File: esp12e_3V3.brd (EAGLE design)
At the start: 50 x 50 mm, 30 parts, among them CN1 1X4-CLEANBIG, CN2 1X4-CLEANBIG, CN3 1X4-CLEANBIG, IC1 117\33

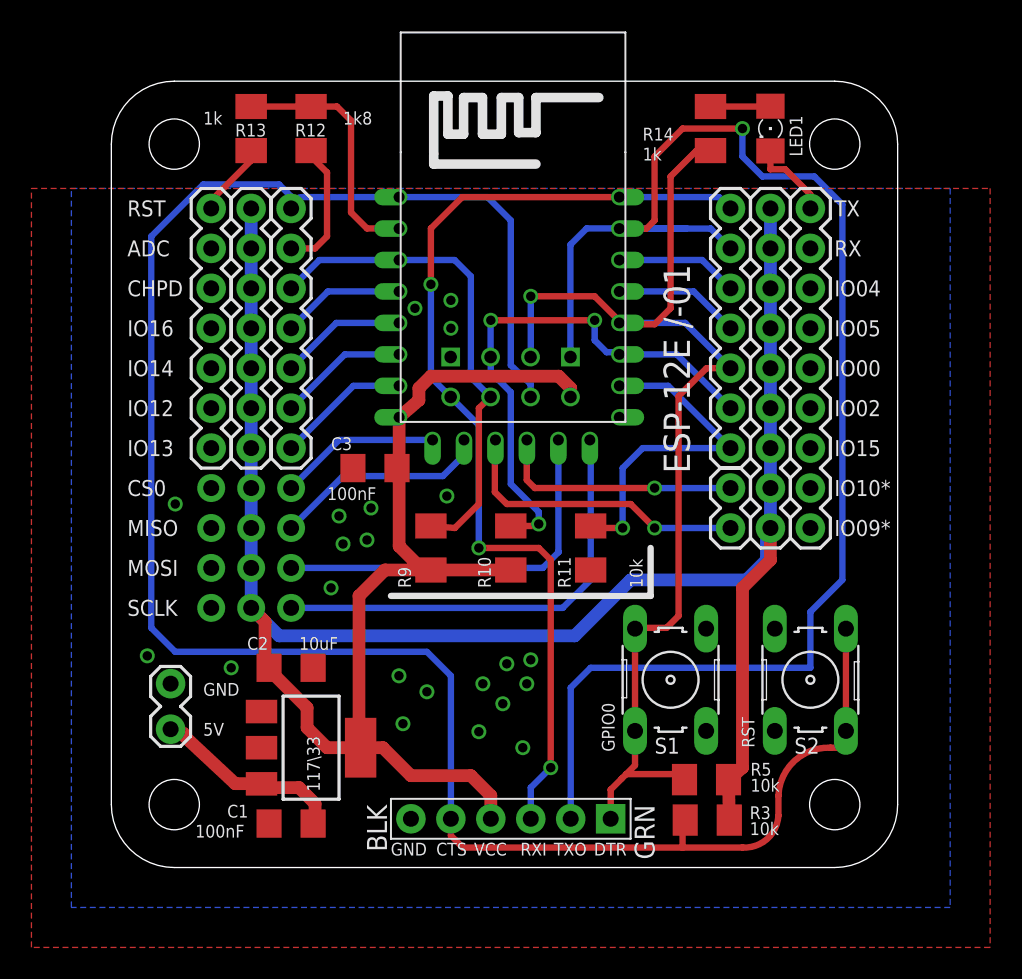
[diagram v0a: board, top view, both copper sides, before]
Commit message: moved 5V header, ftdi and added micro usbfootprint
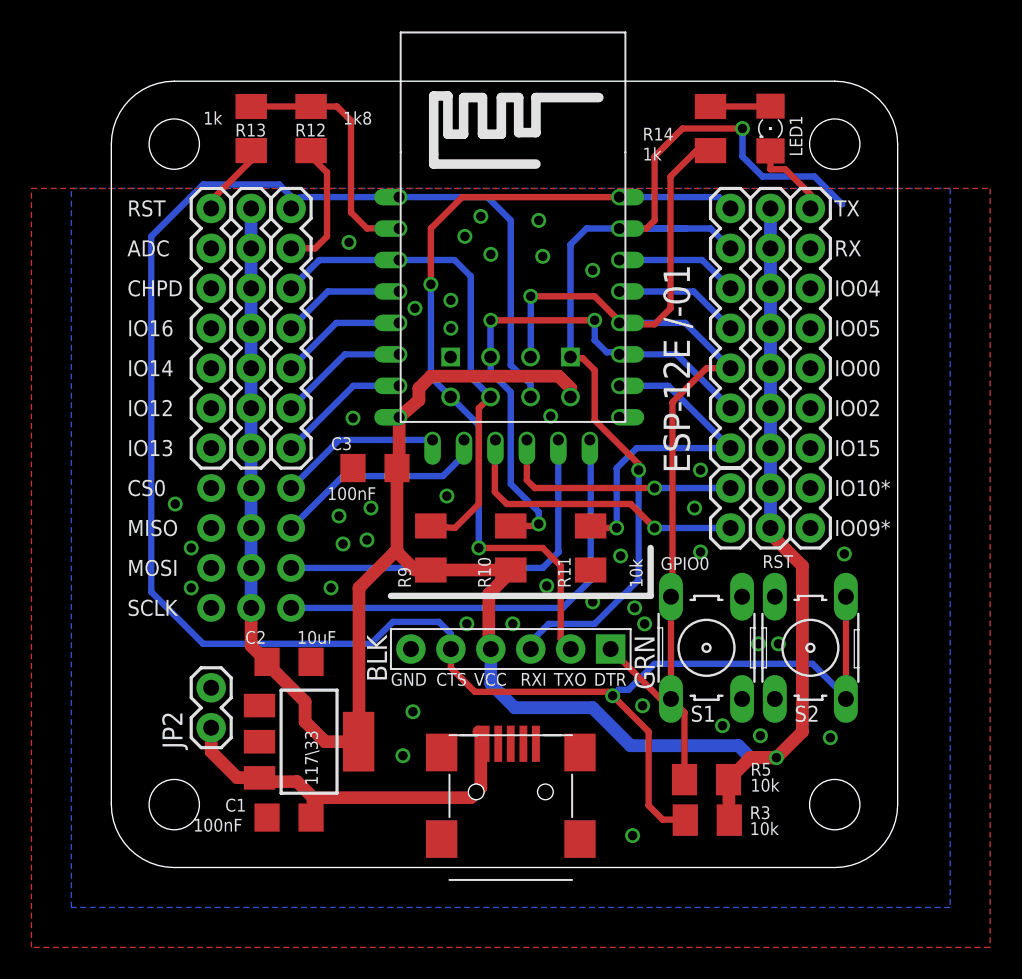
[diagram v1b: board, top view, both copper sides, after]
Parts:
- added CN4: (no value), adafruit:USB-MINIB
- JP2: value M02LOCK -> M02PTH; device SparkFun-Connectors:1X02_LOCK -> SparkFun-Connectors:1X02
- moved JP1 10.8 mm to (25.4, 13.9)
- moved S1 3.06 mm to (37.8, 14.0)
- moved JP2 2.58 mm to (6.35, 8.89)
- moved S2 2.03 mm to (44.5, 14.0)
- moved C2 0.40 mm to (11.3, 13.1)
- moved C1 0.40 mm to (11.3, 3.17)
- moved IC1 0.40 mm to (12.6, 8.00)
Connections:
- removed net FRX_ETX: JP1.P$3, JP5.1, U$2.TX, U$3.TX
- removed net FTX_ERX: JP1.P$2, JP5.2, U$2.RX, U$3.RX
- new net ERX: JP1.P$3, JP5.2, U$2.RX, U$3.RX
- new net ETX: JP1.P$2, JP5.1, U$2.TX, U$3.TX
- net GND: now also CN4.GND
- net VCC: now also CN4.VBUS
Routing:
- net FTX_ERX: track 100.0 -> 0.00 mm, vias 1 -> 0
- net ERX: track 0.00 -> 70.9 mm, vias 0 -> 2
- net FRX_ETX: track 63.6 -> 0.00 mm, vias 3 -> 0
- net ETX: track 0.00 -> 53.0 mm, vias 0 -> 2
- net +3V3: track 175.0 -> 153.8 mm, vias 0 -> 1
- net VCC: track 13.9 -> 26.3 mm
- net GPIO0: track 71.8 -> 68.0 mm
- net N$1: track 131.4 -> 128.9 mm, vias 0 -> 1
- net GND: vias 22 -> 41
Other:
- board text removed: "5V"
- board text removed: "GND"

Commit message: moved stuff
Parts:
- removed CN4: (no value), adafruit:USB-MINIB
- added JP3: USB_MICROB_PLUGCONN-11752, SparkFun-Connectors:USB-B-MICRO-SMD_V03
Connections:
- net GND: now also JP3.GND1; no longer CN4.GND
- net VCC: now also JP3.VBUS1; no longer CN4.VBUS
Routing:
- net VCC: track 26.3 -> 25.1 mm
- net GND: vias 41 -> 48
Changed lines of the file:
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@@
 <element name="CN2" library="adafruit" package="1X04-CLEANBIG" value="1X4-CLEANBIG" x="8.89" y="20.32" smashed="yes" rot="R90"/>
 <element name="CN3" library="adafruit" package="1X04-CLEANBIG" value="1X4-CLEANBIG" x="6.35" y="20.32" smashed="yes" rot="R90"/>
-<element name="CN4" library="adafruit" package="USB-MINIB" value="" x="25.4" y="3.81" smashed="yes">
-<attribute name="VALUE" x="22.09" y="-2.54" size="1.27" layer="27"/>
+<element name="JP2" library="SparkFun-Connectors" package="1X02" value="M02PTH" x="6.35" y="8.89" smashed="yes" rot="R90">
+<attribute name="NAME" x="4.5212" y="7.5438" size="0.8128" layer="25" font="vector" ratio="10" rot="R90"/>
+<attribute name="VALUE" x="9.525" y="7.62" size="1.27" layer="27" rot="R90"/>
 </element>
-<element name="JP2" library="SparkFun-Connectors" package="1X02" value="M02PTH" x="6.35" y="8.89" rot="R90"/>
+<element name="JP3" library="SparkFun-Connectors" package="USB-B-MICRO-SMD_V03" value="USB_MICROB_PLUGCONN-11752" x="25.4" y="2.667" rot="R90">
+<attribute name="PROD_ID" value="CONN-11752" x="25.4" y="2.667" size="1.778" layer="27" rot="R90" display="off"/>
+</element>
 </elements>
 <signals>
@@
 <wire x1="12.827" y1="4.445" x2="12.827" y2="3.045" width="0.8128" layer="1"/>
 <wire x1="12.827" y1="3.045" x2="12.703" y2="3.175" width="0.4064" layer="1"/>
-<contactref element="CN4" pad="VBUS"/>
-<wire x1="12.827" y1="4.445" x2="22.86" y2="4.445" width="0.8128" layer="1"/>
-<wire x1="22.86" y1="4.445" x2="23.495" y2="5.08" width="0.8128" layer="1"/>
-<wire x1="23.495" y1="5.08" x2="23.495" y2="8.509" width="0.8128" layer="1"/>
-<wire x1="23.495" y1="8.509" x2="23.368" y2="8.636" width="0.8128" layer="1"/>
-<wire x1="23.368" y1="8.636" x2="23.368" y2="8.306" width="0.4064" layer="1"/>
-<wire x1="23.368" y1="8.306" x2="23.8" y2="7.874" width="0.4064" layer="1"/>
+<wire x1="12.827" y1="4.445" x2="17.907" y2="4.445" width="0.8128" layer="1"/>
+<wire x1="17.907" y1="4.445" x2="18.542" y2="5.08" width="0.8128" layer="1"/>
+<wire x1="18.542" y1="5.08" x2="18.542" y2="6.223" width="0.8128" layer="1"/>
+<wire x1="18.542" y1="6.223" x2="19.685" y2="7.366" width="0.8128" layer="1"/>
+<wire x1="19.685" y1="7.366" x2="22.606" y2="7.366" width="0.8128" layer="1"/>
+<wire x1="22.606" y1="7.366" x2="23.876" y2="6.096" width="0.8128" layer="1"/>
 <contactref element="JP2" pad="1"/>
 <wire x1="6.35" y1="8.89" x2="6.35" y2="7.366" width="0.8128" layer="1"/>
@@
 <wire x1="8.001" y1="5.715" x2="9.409" y2="5.715" width="0.8128" layer="1"/>
 <wire x1="9.409" y1="5.715" x2="9.423" y2="5.701" width="0.8128" layer="1"/>
+<contactref element="JP3" pad="VBUS1"/>
+<wire x1="23.876" y1="6.096" x2="24.1" y2="5.999" width="0.4064" layer="1"/>
+<wire x1="24.1" y1="5.999" x2="24.1" y2="5.367" width="0.4064" layer="1"/>
 </signal>
 <signal name="GND">
@@
 <via x="21.336" y="23.622" extent="1-16" drill="0.6"/>
 <via x="4.064" y="23.114" extent="1-16" drill="0.6"/>
-<contactref element="CN4" pad="GND"/>
 <via x="37.465" y="20.066" extent="1-16" drill="0.6"/>
 <via x="46.609" y="19.939" extent="1-16" drill="0.6"/>
 <via x="33.909" y="15.494" extent="1-16" drill="0.6"/>
 <via x="32.385" y="19.812" extent="1-16" drill="0.6"/>
-<via x="19.177" y="9.906" extent="1-16" drill="0.6"/>
-<via x="18.542" y="7.112" extent="1-16" drill="0.6"/>
+<via x="32.893" y="5.08" extent="1-16" drill="0.6"/>
 <via x="33.147" y="2.032" extent="1-16" drill="0.6"/>
 <via x="27.94" y="28.702" extent="1-16" drill="0.6"/>
@@
 <via x="23.495" y="41.402" extent="1-16" drill="0.6"/>
 <via x="15.113" y="39.751" extent="1-16" drill="0.6"/>
-<via x="15.367" y="28.575" extent="1-16" drill="0.6"/>
+<via x="13.462" y="24.892" extent="1-16" drill="0.6"/>
 <via x="27.686" y="17.907" extent="1-16" drill="0.6"/>
 <via x="25.527" y="15.494" extent="1-16" drill="0.6"/>
@@
 <via x="30.607" y="37.973" extent="1-16" drill="0.6"/>
 <contactref element="JP2" pad="2"/>
+<contactref element="JP3" pad="GND1"/>
+<via x="30.48" y="7.62" extent="1-16" drill="0.6"/>
+<via x="27.94" y="7.62" extent="1-16" drill="0.6"/>
+<via x="20.32" y="10.16" extent="1-16" drill="0.6"/>
+<via x="17.78" y="10.16" extent="1-16" drill="0.6"/>
+<via x="17.78" y="7.62" extent="1-16" drill="0.6"/>
+<via x="15.494" y="28.702" extent="1-16" drill="0.6"/>
+<via x="25.4" y="7.62" extent="1-16" drill="0.6"/>
+<via x="22.86" y="10.16" extent="1-16" drill="0.6"/>
 </signal>
 <signal name="+3V3">
@@
 <wire x1="23.114" y1="11.176" x2="31.623" y2="11.176" width="0.4064" layer="1"/>
 <wire x1="31.623" y1="11.176" x2="31.877" y2="10.922" width="0.4064" layer="1"/>
-<wire x1="32.8295" y1="9.9695" x2="34.163" y2="8.636" width="0.4064" layer="1"/>
+<wire x1="31.877" y1="10.922" x2="34.163" y2="8.636" width="0.4064" layer="1"/>
 <wire x1="34.163" y1="8.636" x2="34.163" y2="3.937" width="0.4064" layer="1"/>
 <wire x1="34.163" y1="3.937" x2="35.052" y2="3.048" width="0.4064" layer="1"/>
@@
 <wire x1="32.258" y1="11.303" x2="31.877" y2="10.922" width="0.4064" layer="16"/>
 <via x="31.877" y="10.922" extent="1-16" drill="0.6"/>
-<wire x1="31.877" y1="10.922" x2="32.8295" y2="9.9695" width="0.4064" layer="1"/>
 </signal>
 <signal name="N$2">

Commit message: removed "antenna" - wire on pcb and pulled usb
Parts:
- moved JP3 0.25 mm to (25.4, 2.41)
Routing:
- net ERX: track 70.9 -> 48.7 mm, vias 2 -> 1
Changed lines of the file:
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@@
 <attribute name="VALUE" x="9.525" y="7.62" size="1.27" layer="27" rot="R90"/>
 </element>
-<element name="JP3" library="SparkFun-Connectors" package="USB-B-MICRO-SMD_V03" value="USB_MICROB_PLUGCONN-11752" x="25.4" y="2.667" rot="R90">
-<attribute name="PROD_ID" value="CONN-11752" x="25.4" y="2.667" size="1.778" layer="27" rot="R90" display="off"/>
+<element name="JP3" library="SparkFun-Connectors" package="USB-B-MICRO-SMD_V03" value="USB_MICROB_PLUGCONN-11752" x="25.4" y="2.413" rot="R90">
+<attribute name="PROD_ID" value="CONN-11752" x="25.4" y="2.413" size="1.778" layer="27" rot="R90" display="off"/>
 </element>
 </elements>
@@
 <contactref element="JP3" pad="VBUS1"/>
 <wire x1="23.876" y1="6.096" x2="24.1" y2="5.999" width="0.4064" layer="1"/>
-<wire x1="24.1" y1="5.999" x2="24.1" y2="5.367" width="0.4064" layer="1"/>
+<wire x1="24.1" y1="5.999" x2="24.1" y2="5.113" width="0.4064" layer="1"/>
 </signal>
 <signal name="GND">
@@
 <wire x1="38.1" y1="40.64" x2="38.1" y2="40.63" width="0.254" layer="16"/>
 <wire x1="36.576" y1="40.64" x2="33.02" y2="40.64" width="0.4064" layer="16"/>
-<wire x1="46.482" y1="42.164" x2="44.704" y2="43.942" width="0.4064" layer="16"/>
-<wire x1="44.704" y1="43.942" x2="41.402" y2="43.942" width="0.4064" layer="16"/>
-<wire x1="41.402" y1="43.942" x2="40.132" y2="45.212" width="0.4064" layer="16"/>
-<wire x1="40.132" y1="45.212" x2="40.132" y2="46.99" width="0.4064" layer="16"/>
-<via x="40.132" y="46.99" extent="1-16" drill="0.6"/>
-<wire x1="40.132" y1="46.99" x2="36.322" y2="46.99" width="0.4064" layer="1"/>
-<wire x1="36.322" y1="46.99" x2="34.544" y2="45.212" width="0.4064" layer="1"/>
-<wire x1="34.544" y1="45.212" x2="34.544" y2="41.148" width="0.4064" layer="1"/>
-<wire x1="34.544" y1="41.148" x2="34.036" y2="40.63" width="0.4064" layer="1"/>
-<wire x1="34.036" y1="40.63" x2="32.3" y2="40.63" width="0.4064" layer="1"/>
 <contactref element="JP1" pad="P$3"/>
 <wire x1="26.67" y1="13.8938" x2="26.67" y2="14.351" width="0.4064" layer="16"/>

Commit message: kitnic.it stuff
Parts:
- removed JP2: M02PTH, SparkFun-Connectors:1X02
- added JP6: (no value), pinhead:1X03
- R12: value 1k8 -> 39k
- R13: value 1k -> 10k
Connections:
- net +3V3: now also JP6.3
- net GND: now also JP6.2; no longer JP2.2
- net VCC: now also JP6.1; no longer JP2.1
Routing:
- net N$1: track 128.9 -> 121.3 mm
- net +3V3: track 153.8 -> 159.9 mm
- net VCC: track 25.4 -> 27.0 mm
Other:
- board text added: "3V3"
- board text added: "5V"
- board text added: "GND"
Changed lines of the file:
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@@
 <text x="1.016" y="16.002" size="1.016" layer="25" font="vector">SCLK</text>
 <text x="13.716" y="23.368" size="0.8128" layer="25" font="vector">100nF</text>
+<text x="2.032" y="12.954" size="0.8128" layer="25" font="vector" rot="R90">3V3</text>
+<text x="2.032" y="10.414" size="0.8128" layer="25" font="vector" rot="R90">GND</text>
+<text x="2.032" y="8.128" size="0.8128" layer="25" font="vector" rot="R90">5V</text>
 </plain>
 <attributes>
@@
 <attribute name="VALUE" x="33.782" y="17.78" size="0.8128" layer="25" font="vector" rot="R90"/>
 </element>
-<element name="R12" library="resistor" package="M1206" value="1k8" x="12.7" y="46.99" smashed="yes" rot="R90">
+<element name="R12" library="resistor" package="M1206" value="39k" x="12.7" y="46.99" smashed="yes" rot="R90">
 <attribute name="NAME" x="11.684" y="46.482" size="0.8128" layer="25" font="vector"/>
 <attribute name="VALUE" x="14.732" y="47.244" size="0.8128" layer="25" font="vector"/>
 </element>
-<element name="R13" library="resistor" package="M1206" value="1k" x="8.89" y="46.99" smashed="yes" rot="R270">
+<element name="R13" library="resistor" package="M1206" value="10k" x="8.89" y="46.99" smashed="yes" rot="R270">
 <attribute name="NAME" x="7.874" y="46.482" size="0.8128" layer="25" font="vector"/>
 <attribute name="VALUE" x="5.842" y="47.244" size="0.8128" layer="25" font="vector"/>
@@
 <element name="CN2" library="adafruit" package="1X04-CLEANBIG" value="1X4-CLEANBIG" x="8.89" y="20.32" smashed="yes" rot="R90"/>
 <element name="CN3" library="adafruit" package="1X04-CLEANBIG" value="1X4-CLEANBIG" x="6.35" y="20.32" smashed="yes" rot="R90"/>
-<element name="JP2" library="SparkFun-Connectors" package="1X02" value="M02PTH" x="6.35" y="8.89" smashed="yes" rot="R90">
-<attribute name="NAME" x="4.5212" y="7.5438" size="0.8128" layer="25" font="vector" ratio="10" rot="R90"/>
-<attribute name="VALUE" x="9.525" y="7.62" size="1.27" layer="27" rot="R90"/>
-</element>
 <element name="JP3" library="SparkFun-Connectors" package="USB-B-MICRO-SMD_V03" value="USB_MICROB_PLUGCONN-11752" x="25.4" y="2.413" rot="R90">
 <attribute name="PROD_ID" value="CONN-11752" x="25.4" y="2.413" size="1.778" layer="27" rot="R90" display="off"/>
+</element>
+<element name="JP6" library="pinhead" package="1X03" value="" x="3.81" y="11.43" smashed="yes" rot="R90">
+<attribute name="VALUE" x="6.985" y="7.62" size="1.27" layer="27" rot="R90"/>
 </element>
 </elements>
@@
 <wire x1="19.685" y1="7.366" x2="22.606" y2="7.366" width="0.8128" layer="1"/>
 <wire x1="22.606" y1="7.366" x2="23.876" y2="6.096" width="0.8128" layer="1"/>
-<contactref element="JP2" pad="1"/>
-<wire x1="6.35" y1="8.89" x2="6.35" y2="7.366" width="0.8128" layer="1"/>
-<wire x1="6.35" y1="7.366" x2="8.001" y2="5.715" width="0.8128" layer="1"/>
+<wire x1="4.826" y1="8.89" x2="8.001" y2="5.715" width="0.8128" layer="1"/>
 <wire x1="8.001" y1="5.715" x2="9.409" y2="5.715" width="0.8128" layer="1"/>
 <wire x1="9.409" y1="5.715" x2="9.423" y2="5.701" width="0.8128" layer="1"/>
@@
 <wire x1="23.876" y1="6.096" x2="24.1" y2="5.999" width="0.4064" layer="1"/>
 <wire x1="24.1" y1="5.999" x2="24.1" y2="5.113" width="0.4064" layer="1"/>
+<contactref element="JP6" pad="1"/>
+<wire x1="3.81" y1="8.89" x2="4.826" y2="8.89" width="0.8128" layer="1"/>
 </signal>
 <signal name="GND">
@@
 <via x="33.782" y="10.287" extent="1-16" drill="0.6"/>
 <via x="30.607" y="37.973" extent="1-16" drill="0.6"/>
-<contactref element="JP2" pad="2"/>
 <contactref element="JP3" pad="GND1"/>
 <via x="30.48" y="7.62" extent="1-16" drill="0.6"/>
@@
 <via x="25.4" y="7.62" extent="1-16" drill="0.6"/>
 <via x="22.86" y="10.16" extent="1-16" drill="0.6"/>
+<contactref element="JP6" pad="2"/>
 </signal>
 <signal name="+3V3">
@@
 <wire x1="24.003" y1="17.399" x2="24.003" y2="14.0208" width="0.8128" layer="1"/>
 <wire x1="24.003" y1="14.0208" x2="24.13" y2="13.8938" width="0.8128" layer="1"/>
+<contactref element="JP6" pad="3"/>
+<wire x1="3.81" y1="13.97" x2="6.35" y2="13.97" width="0.8128" layer="1"/>
+<wire x1="6.35" y1="13.97" x2="8.89" y2="16.51" width="0.8128" layer="1"/>
 </signal>
 <signal name="ERX">
@@
 </signal>
 <signal name="N$1">
-<wire x1="2.54" y1="17.526" x2="2.54" y2="40.132" width="0.4064" layer="16"/>
-<wire x1="2.54" y1="40.132" x2="5.842" y2="43.434" width="0.4064" layer="16"/>
-<wire x1="5.842" y1="43.434" x2="10.668" y2="43.434" width="0.4064" layer="16"/>
-<wire x1="10.668" y1="43.434" x2="11.43" y2="42.672" width="0.4064" layer="16"/>
+<wire x1="7.62" y1="15.621" x2="7.62" y2="42.672" width="0.3048" layer="16"/>
+<wire x1="7.62" y1="42.672" x2="8.509" y2="43.434" width="0.3048" layer="16"/>
+<wire x1="8.509" y1="43.434" x2="10.668" y2="43.434" width="0.3048" layer="16"/>
+<wire x1="10.668" y1="43.434" x2="11.43" y2="42.672" width="0.3048" layer="16"/>
 <contactref element="U$2" pad="RST"/>
 <contactref element="U$3" pad="RESET"/>
@@
 <contactref element="R3" pad="2"/>
 <contactref element="JP4" pad="7"/>
-<wire x1="18.3" y1="42.63" x2="12.15" y2="42.63" width="0.4064" layer="16"/>
+<wire x1="18.3" y1="42.63" x2="12.15" y2="42.63" width="0.3048" layer="16"/>
 <wire x1="12.15" y1="42.63" x2="11.43" y2="41.91" width="0.4064" layer="16" curve="90"/>
 <wire x1="18.3" y1="42.63" x2="23.918" y2="42.63" width="0.4064" layer="16"/>
@@
 <wire x1="26.655" y1="30.719" x2="26.655" y2="29.9225" width="0.4064" layer="16"/>
 <contactref element="JP1" pad="P$5"/>
-<wire x1="11.43" y1="42.672" x2="11.43" y2="41.91" width="0.4064" layer="16"/>
+<wire x1="11.43" y1="42.672" x2="11.43" y2="41.91" width="0.3048" layer="16"/>
 <wire x1="46.7106" y1="17.2212" x2="46.7106" y2="10.7188" width="0.4064" layer="1"/>
 <wire x1="21.59" y1="13.8938" x2="21.59" y2="14.859" width="0.4064" layer="16"/>
@@
 <wire x1="20.828" y1="15.621" x2="17.907" y2="15.621" width="0.4064" layer="16"/>
 <wire x1="17.907" y1="15.621" x2="16.51" y2="14.224" width="0.4064" layer="16"/>
-<wire x1="16.51" y1="14.224" x2="5.842" y2="14.224" width="0.4064" layer="16"/>
-<wire x1="5.842" y1="14.224" x2="2.54" y2="17.526" width="0.4064" layer="16"/>
+<wire x1="16.51" y1="14.224" x2="9.017" y2="14.224" width="0.4064" layer="16"/>
+<wire x1="9.017" y1="14.224" x2="7.62" y2="15.621" width="0.4064" layer="16"/>
 <wire x1="21.59" y1="13.8938" x2="21.59" y2="12.7" width="0.4064" layer="1"/>
 <wire x1="21.59" y1="12.7" x2="23.114" y2="11.176" width="0.4064" layer="1"/>
